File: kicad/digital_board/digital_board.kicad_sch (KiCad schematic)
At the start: 94 parts

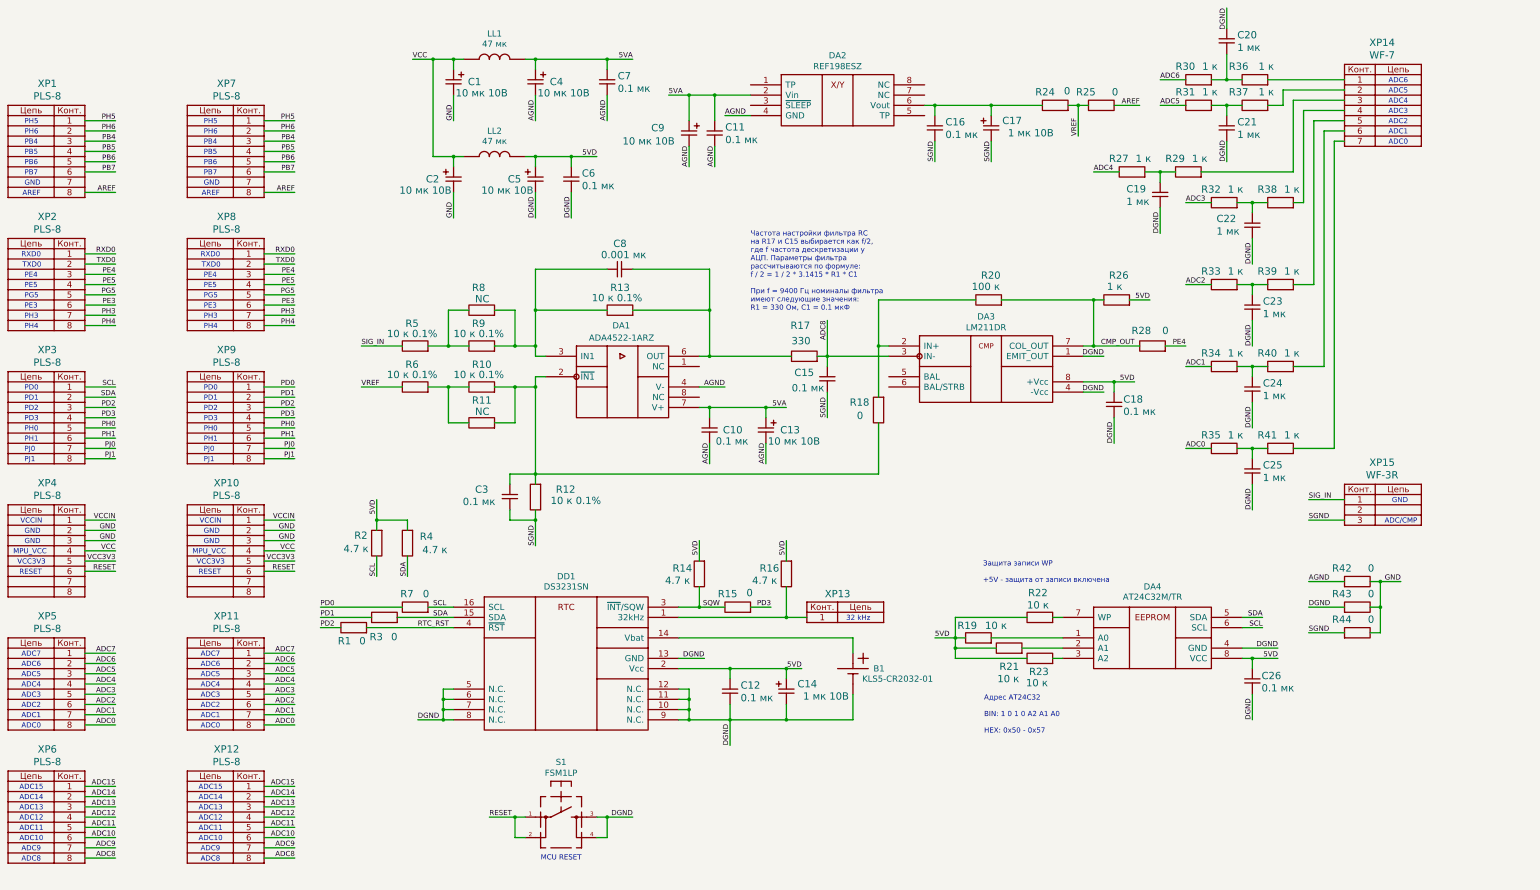
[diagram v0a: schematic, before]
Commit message: Приступил к трассировке печатной платы.
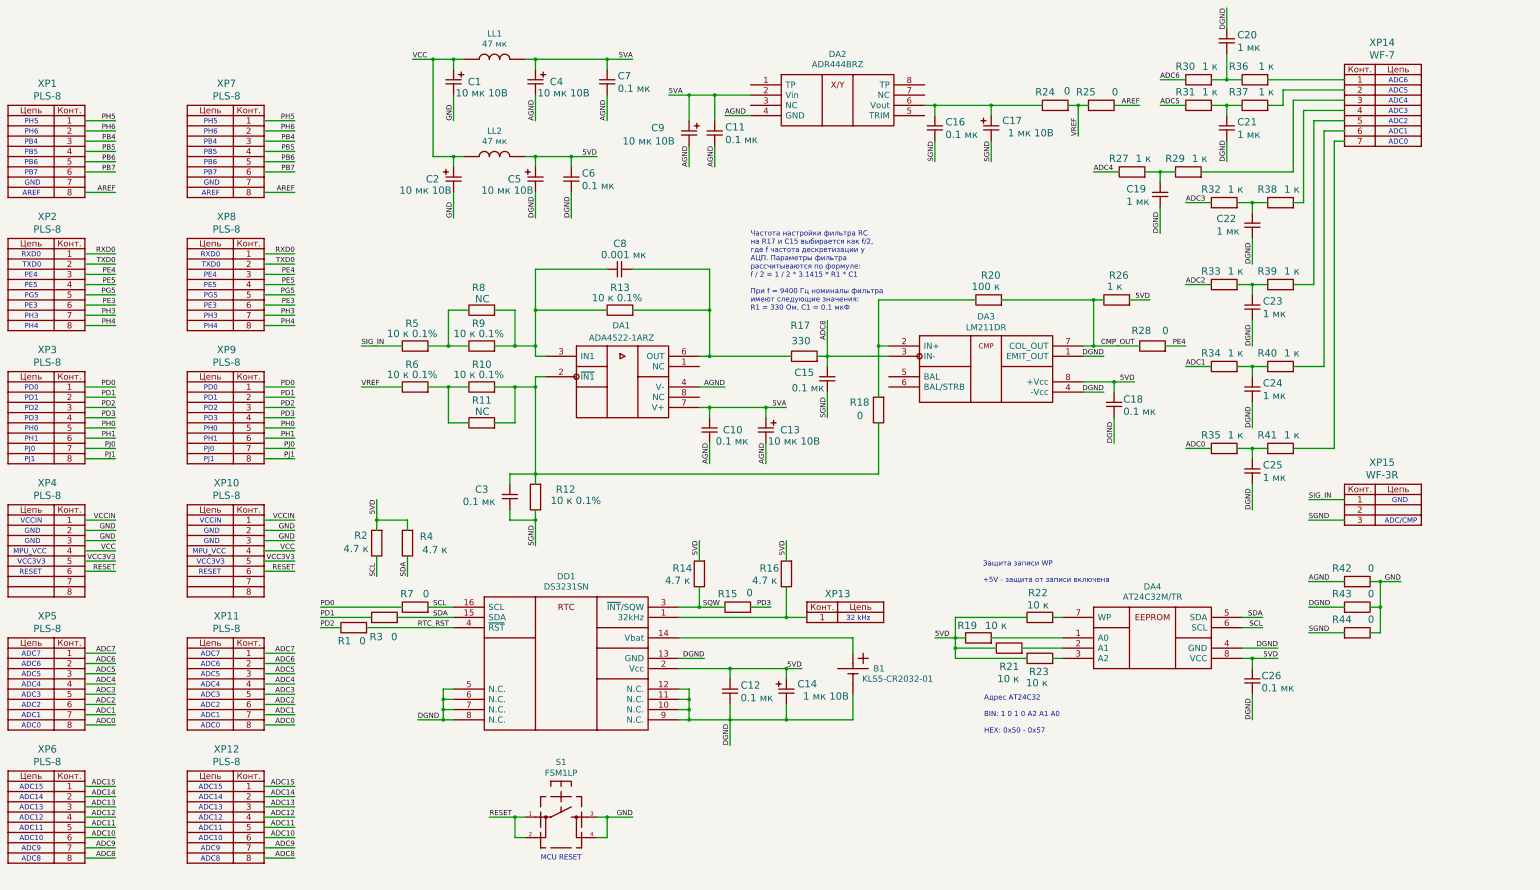
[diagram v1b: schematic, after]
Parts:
- removed DA2: REF198ESZ, IWsmd_case:SOIC8, symbol LFcomponents:REF19x
- added DA2: ADR444BRZ, IWsmd_case:SOIC8, symbol LFcomponents:ADR44x
- B1: footprint (none) -> IWcomponents:KLS5-CR2032-01
- C1, C13, C14, C17, C2, C4, C5, C9: footprint (none) -> IWsmd_case:CASE_A
- DA1, DA4: footprint (none) -> IWsmd_case:SOIC8
- DD1: footprint (none) -> IWsmd_case:SOIC16_RW16
- LL1, LL2: footprint (none) -> IWsmd_case:SMD0805
- XP13: footprint IWconnectors:WF-1 -> IWconnectors:1_pin_1_0mm
- XP15: footprint IWconnectors:WF-3 -> IWconnectors:WF-3R
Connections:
- net 5VA: now also DA2.2 (Vin)
- net AGND: now also DA2.4 (GND)
- net DGND: no longer S1.3, S1.4
- net GND: now also S1.3, S1.4
- net PD0: now also XP3.1
- net PD1: now also XP3.2
- net SCL: no longer XP3.1
- net SDA: no longer XP3.2
- net at C16.1, C17.1, R24.2: now also DA2.6 (Vout)
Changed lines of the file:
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@@
 		)
 	)
-	(label "SDA"
+	(label "PD1"
 		(at 76.2 114.3 180)
 		(effects
@@
 		)
 	)
-	(label "DGND"
+	(label "GND"
 		(at 204.47 218.44 180)
 		(effects
@@
 		)
 	)
-	(label "SCL"
+	(label "PD0"
 		(at 76.2 111.76 180)
 		(effects
@@
 	)
 	(symbol
-		(lib_id "LFcomponents:REF19x")
-		(at 241.3 34.29 0)
-		(unit 1)
-		(exclude_from_sim no)
-		(in_bom yes)
-		(on_board yes)
-		(dnp no)
-		(property "Reference" "DA2"
-			(at 255.27 29.5402 0)
-			(effects
-				(font
-					(size 1.524 1.524)
-				)
-			)
-		)
-		(property "Value" "REF198ESZ"
-			(at 255.27 32.2326 0)
-			(effects
-				(font
-					(size 1.524 1.524)
-				)
-			)
-		)
-		(property "Footprint" "IWsmd_case:SOIC8"
-			(at 241.3 34.29 0)
-			(effects
-				(font
-					(size 1.524 1.524)
-				)
-				(hide yes)
-			)
-		)
-		(property "Datasheet" ""
-			(at 241.3 34.29 0)
-			(effects
-				(font
-					(size 1.524 1.524)
-				)
-			)
-		)
-		(property "Description" ""
-			(at 241.3 34.29 0)
-			(effects
-				(font
-					(size 1.27 1.27)
-				)
-			)
-		)
-		(pin "1"
-		)
-		(pin "2"
-		)
-		(pin "3"
-		)
-		(pin "4"
-		)
-		(pin "5"
-		)
-		(pin "6"
-		)
-		(pin "7"
-		)
-		(pin "8"
-		)
-		(instances
-			(project "digital_board"
-				(path "/904f87ef-2bbd-4cec-934f-2ccbfdfb4c4a"
-					(reference "DA2")
-					(unit 1)
-				)
-			)
-		)
-	)
-	(symbol
 		(lib_id "LFbutton:KLS7-TS6601-XX")
 		(at 177.8 218.44 0)
@@
 			)
 		)
-		(property "Footprint" "IWconnectors:WF-3"
+		(property "Footprint" "IWconnectors:WF-3R"
 			(at 389.89 135.89 0)
 			(effects
@@
 			)
 		)
-		(property "Footprint" "IWconnectors:WF-1"
+		(property "Footprint" "IWconnectors:1_pin_1_0mm"
 			(at 256.54 165.1 0)
 			(effects
@@
 			)
 		)
-		(property "Footprint" ""
+		(property "Footprint" "IWsmd_case:SOIC8"
 			(at 191.77 101.6 0)
 			(effects
@@
 					(size 1.524 1.524)
 				)
+				(hide yes)
 			)
 		)
@@
 			)
 		)
-		(property "Footprint" ""
+		(property "Footprint" "IWsmd_case:CASE_A"
 			(at 237.49 119.38 0)
 			(effects
@@
 			)
 		)
-		(property "Footprint" ""
+		(property "Footprint" "IWsmd_case:SOIC8"
 			(at 318.77 166.37 0)
 			(effects
@@
 					(size 1.524 1.524)
 				)
+				(hide yes)
 			)
 		)
@@
 			)
 		)
-		(property "Footprint" ""
+		(property "Footprint" "IWsmd_case:CASE_A"
 			(at 160.02 57.15 0)
 			(effects
@@
 			)
 		)
-		(property "Footprint" ""
+		(property "Footprint" "IWsmd_case:CASE_A"
 			(at 180.34 57.15 0)
 			(effects
@@
 			)
 		)
-		(property "Footprint" ""
+		(property "Footprint" "IWsmd_case:SOIC16_RW16"
 			(at 167.64 163.83 0)
 			(effects
@@
 					(size 1.524 1.524)
 				)
+				(hide yes)
 			)
 		)
@@
 			)
 		)
-		(property "Footprint" ""
+		(property "Footprint" "IWsmd_case:CASE_A"
 			(at 242.57 184.15 0)
 			(effects
@@
 			)
 		)
-		(property "Footprint" ""
+		(property "Footprint" "IWsmd_case:SMD0805"
 			(at 177.8 54.61 0)
 			(effects
@@
 					(size 1.524 1.524)
 				)
+				(hide yes)
 			)
 		)
@@
 			)
 		)
-		(property "Footprint" ""
+		(property "Footprint" "IWsmd_case:SMD0805"
 			(at 162.56 30.48 0)
 			(effects
@@
 					(size 1.524 1.524)
 				)
+				(hide yes)
 			)
 		)
@@
 	)
 	(symbol
+		(lib_id "LFcomponents:ADR44x")
+		(at 241.3 34.29 0)
+		(unit 1)
+		(exclude_from_sim no)
+		(in_bom yes)
+		(on_board yes)
+		(dnp no)
+		(fields_autoplaced yes)
+		(property "Reference" "DA2"
+			(at 255.27 29.21 0)
+			(effects
+				(font
+					(size 1.524 1.524)
+				)
+			)
+		)
+		(property "Value" "ADR444BRZ"
+			(at 255.27 31.75 0)
+			(effects
+				(font
+					(size 1.524 1.524)
+				)
+			)
+		)
+		(property "Footprint" "IWsmd_case:SOIC8"
+			(at 241.3 34.29 0)
+			(effects
+				(font
+					(size 1.524 1.524)
+				)
+				(hide yes)
+			)
+		)
+		(property "Datasheet" ""
+			(at 241.3 34.29 0)
+			(effects
+				(font
+					(size 1.524 1.524)
+				)
+			)
+		)
+		(property "Description" ""
+			(at 241.3 34.29 0)
+			(effects
+				(font
+					(size 1.27 1.27)
+				)
+				(hide yes)
+			)
+		)
+		(pin "6"
+		)
+		(pin "5"
+		)
+		(pin "7"
+		)
+		(pin "4"
+		)
+		(pin "8"
+		)
+		(pin "1"
+		)
+		(pin "2"
+		)
+		(pin "3"
+		)
+		(instances
+			(project ""
+				(path "/904f87ef-2bbd-4cec-934f-2ccbfdfb4c4a"
+					(reference "DA2")
+					(unit 1)
+				)
+			)
+		)
+	)
+	(symbol
 		(lib_id "LFcapitors:CAPITORS_ELECTROLYTIC")
 		(at 293.37 44.45 90)
@@
 			)
 		)
-		(property "Footprint" ""
+		(property "Footprint" "IWsmd_case:CASE_A"
 			(at 293.37 44.45 0)
 			(effects
@@
 			)
 		)
-		(property "Footprint" ""
+		(property "Footprint" "IWsmd_case:CASE_A"
 			(at 180.34 33.02 0)
 			(effects
@@
 			)
 		)
-		(property "Footprint" ""
+		(property "Footprint" "IWsmd_case:CASE_A"
 			(at 218.44 45.72 0)
 			(effects
@@
 			)
 		)
-		(property "Footprint" ""
+		(property "Footprint" "IWcomponents:KLS5-CR2032-01"
 			(at 259.08 177.8 0)
 			(effects
@@
 					(size 1.524 1.524)
 				)
+				(hide yes)
 			)
 		)
@@
 			)
 		)
-		(property "Footprint" ""
+		(property "Footprint" "IWsmd_case:CASE_A"
 			(at 160.02 33.02 0)
 			(effects

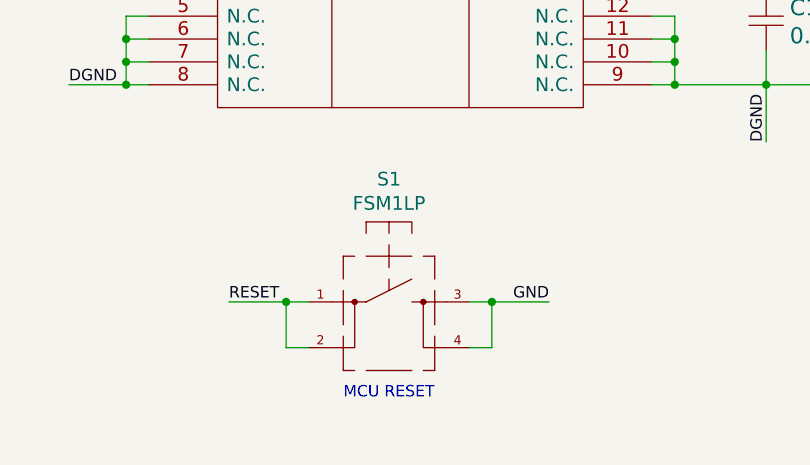
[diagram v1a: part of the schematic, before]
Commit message: Закончил трассировку цифровой печатной платы.
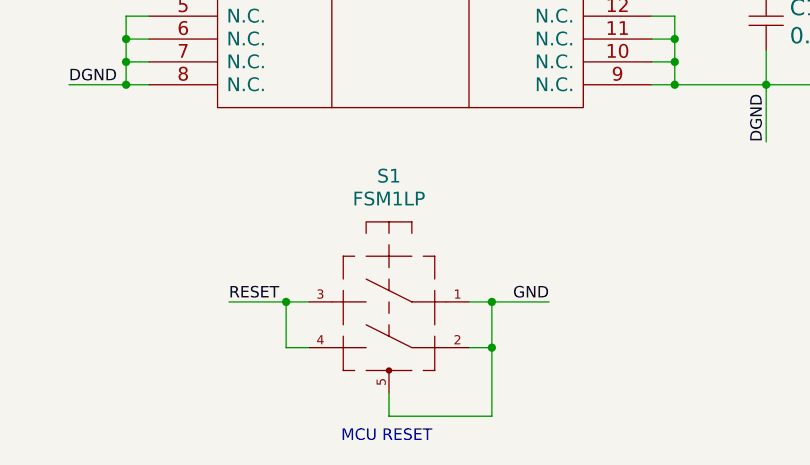
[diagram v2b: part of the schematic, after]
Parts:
- removed S1: FSM1LP, IWsmd_case:SWD_BUTTON, symbol LFbutton:KLS7-TS6601-XX
- added S1: FSM1LP, IWsmd_case:SWD_BUTTON, symbol LFbutton:button_smd_1
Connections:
- net GND: now also S1.1, S1.2, S1.5
- net RESET: now also S1.3, S1.4
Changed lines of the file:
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@@
 	(text "MCU RESET"
 		(exclude_from_sim no)
-		(at 186.69 228.6 0)
+		(at 186.436 233.426 0)
 		(effects
 			(font
@@
 	)
 	(junction
+		(at 198.12 223.52)
+		(diameter 0)
+		(color 0 0 0 0)
+	)
+	(junction
 		(at 284.48 176.53)
 		(diameter 0)
@@
 	(wire
 		(pts
+			(xy 198.12 231.14) (xy 198.12 223.52)
+		)
+		(stroke
+			(width 0)
+			(type default)
+		)
+	)
+	(wire
+		(pts
 			(xy 355.6 168.91) (xy 360.68 168.91)
 		)
@@
 	(wire
 		(pts
+			(xy 186.69 228.6) (xy 186.69 231.14)
+		)
+		(stroke
+			(width 0)
+			(type default)
+		)
+	)
+	(wire
+		(pts
 			(xy 68.58 180.34) (xy 76.2 180.34)
 		)
@@
 	(wire
 		(pts
+			(xy 186.69 231.14) (xy 198.12 231.14)
+		)
+		(stroke
+			(width 0)
+			(type default)
+		)
+	)
+	(wire
+		(pts
 			(xy 215.9 173.99) (xy 259.08 173.99)
 		)
@@
 	)
 	(symbol
-		(lib_id "LFbutton:KLS7-TS6601-XX")
-		(at 177.8 218.44 0)
-		(unit 1)
-		(exclude_from_sim no)
-		(in_bom yes)
-		(on_board yes)
-		(dnp no)
-		(property "Reference" "S1"
-			(at 186.69 204.8002 0)
-			(effects
-				(font
-					(size 1.524 1.524)
-				)
-			)
-		)
-		(property "Value" "FSM1LP"
-			(at 186.69 207.4926 0)
-			(effects
-				(font
-					(size 1.524 1.524)
-				)
-			)
-		)
-		(property "Footprint" "IWsmd_case:SWD_BUTTON"
-			(at 177.8 218.44 0)
-			(effects
-				(font
-					(size 1.524 1.524)
-				)
-				(hide yes)
-			)
-		)
-		(property "Datasheet" ""
-			(at 177.8 218.44 0)
-			(effects
-				(font
-					(size 1.524 1.524)
-				)
-			)
-		)
-		(property "Description" ""
-			(at 177.8 218.44 0)
-			(effects
-				(font
-					(size 1.27 1.27)
-				)
-			)
-		)
-		(pin "1"
-		)
-		(pin "2"
-		)
-		(pin "3"
-		)
-		(pin "4"
-		)
-		(instances
-			(project "digital_board"
-				(path "/904f87ef-2bbd-4cec-934f-2ccbfdfb4c4a"
-					(reference "S1")
-					(unit 1)
-				)
-			)
-		)
-	)
-	(symbol
 		(lib_id "LFconnectors:connector_8pin_gost")
 		(at 68.58 45.72 0)
@@
 					(unit 1)
 				)
+			)
+		)
+	)
+	(symbol
+		(lib_id "LFbutton:button_smd_1")
+		(at 195.58 218.44 0)
+		(mirror y)
+		(unit 1)
+		(exclude_from_sim no)
+		(in_bom yes)
+		(on_board yes)
+		(dnp no)
+		(property "Reference" "S1"
+			(at 186.69 204.47 0)
+			(effects
+				(font
+					(size 1.524 1.524)
+				)
+			)
+		)
+		(property "Value" "FSM1LP"
+			(at 186.69 207.01 0)
+			(effects
+				(font
+					(size 1.524 1.524)
+				)
+			)
+		)
+		(property "Footprint" "IWsmd_case:SWD_BUTTON"
+			(at 195.58 218.44 0)
+			(effects
+				(font
+					(size 1.524 1.524)
+				)
+				(hide yes)
+			)
+		)
+		(property "Datasheet" ""
+			(at 195.58 218.44 0)
+			(effects
+				(font
+					(size 1.524 1.524)
+				)
+			)
+		)
+		(property "Description" ""
+			(at 195.58 218.44 0)
+			(effects
+				(font
+					(size 1.27 1.27)
+				)
+				(hide yes)
+			)
+		)
+		(pin "3"
+		)
+		(pin "5"
+		)
+		(pin "1"
+		)
+		(pin "2"
+		)
+		(pin "4"
+		)
+		(instances
+			(project ""
+				(path "/904f87ef-2bbd-4cec-934f-2ccbfdfb4c4a"
+					(reference "S1")
+					(unit 1)
+				)

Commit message: Закончил проверку работоспособности цифровой платы.
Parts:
- C19, C20, C21, C22, C23, C24, C25: value 1 мк -> 100 п
- C8: value 0.001 мк -> 1 н
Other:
- note added: "!Перепутано подключение к 2 и 3 ногам DA1"
- note added: "1) Вместо R18 нужно добавить делитель из двух резисторов по 100 кОм от систочника опорного напряжения AREF. К резистору идущему на землю SGND нужно добавить керамический чип конденсатор 0.1 мкФ. Резистор обратной связи компаратора R20 у DA3 впаивать не нунужно, наличие резустора приводит к искажению в сигнале с ОУ DA1 и многократному срабатыванию компаратора на фронтах выходного сигнала. 2) На вы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"
- note added: "Если нет ложного срабатывания кнопок у клавиатуры то конденсаторы Т-образных НЧ фильтров впаивать не нужно, а все резисторы фильтров нужно заменить на перемычки 0 Ом."
